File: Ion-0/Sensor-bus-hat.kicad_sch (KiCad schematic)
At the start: 98 parts, among them J10 Conn_CAN, J13 Conn_01x04, J15 Conn_01x04, J6 Coaxial_Small, J7 Conn_Probs, J8 Conn_Heater, Q1 IRLML6244, Q2 IRLML6244, U1 HDC2080, U2 MS5607-02BA, U3 BNO085, U4 TCA9617ADGKR, U5 A4988SETTR-T, U6 MAX-M10M-00B, U7 TPS3850H50DRCR, U8 SN65HVD230, Y2 9HT10-32.768KBZF-T

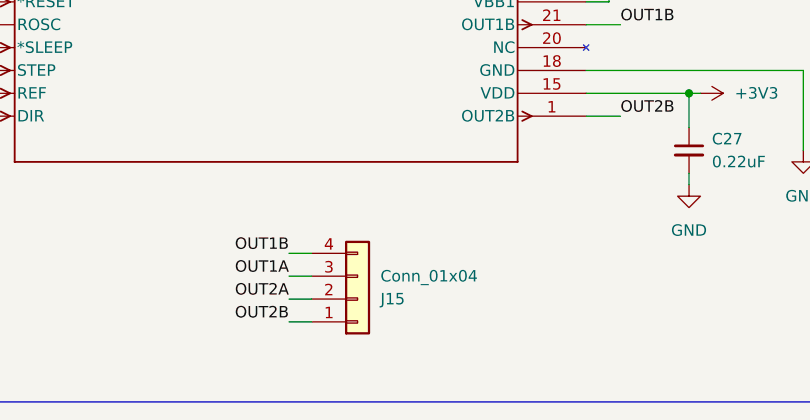
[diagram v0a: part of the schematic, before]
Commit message: silkscreen changes
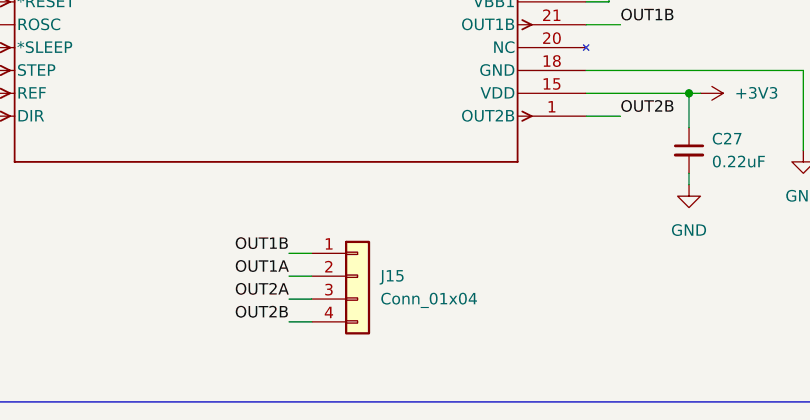
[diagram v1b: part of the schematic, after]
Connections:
- net OUT1A: now also J15.2 (Pin_2); no longer J15.3 (Pin_3)
- net OUT1B: now also J15.1 (Pin_1); no longer J15.4 (Pin_4)
- net OUT2A: now also J15.3 (Pin_3); no longer J15.2 (Pin_2)
- net OUT2B: now also J15.4 (Pin_4); no longer J15.1 (Pin_1)
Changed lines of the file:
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@@
 	(symbol
 		(lib_id "Connector_Generic:Conn_01x04")
-		(at 102.87 270.51 0)
-		(mirror x)
+		(at 102.87 267.97 0)
 		(unit 1)
 		(body_style 1)
@@
 		(dnp no)
 		(property "Reference" "J15"
-			(at 105.41 270.5101 0)
+			(at 105.41 267.9699 0)
 			(show_name no)
 			(do_not_autoplace no)
@@
 		)
 		(property "Value" "Conn_01x04"
-			(at 105.41 267.9701 0)
+			(at 105.41 270.5099 0)
 			(show_name no)
 			(do_not_autoplace no)
@@
 		)
 		(property "Footprint" "Connector_JST:JST_XH_B4B-XH-AM_1x04_P2.50mm_Vertical"
-			(at 102.87 270.51 0)
+			(at 102.87 267.97 0)
 			(hide yes)
 			(show_name no)
@@
 		)
 		(property "Datasheet" ""
-			(at 102.87 270.51 0)
+			(at 102.87 267.97 0)
 			(hide yes)
 			(show_name no)
@@
 		)
 		(property "Description" "Generic connector, single row, 01x04, script generated (kicad-library-utils/schlib/autogen/connector/)"
-			(at 102.87 270.51 0)
+			(at 102.87 267.97 0)
 			(hide yes)
 			(show_name no)

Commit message: fixed impedance mismatch
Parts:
- C11: footprint Capacitor_SMD:C_0603_1608Metric -> Capacitor_SMD:C_0402_1005Metric
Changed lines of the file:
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@@
 			)
 		)
-		(property "Footprint" "Capacitor_SMD:C_0603_1608Metric"
+		(property "Footprint" "Capacitor_SMD:C_0402_1005Metric"
 			(at 198.12 179.07 0)
 			(hide yes)

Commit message: BOM ORDER
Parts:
- removed R12: 523, Resistor_SMD:R_0603_1608Metric_Pad0.98x0.95mm_HandSolder, symbol Device:R_Small_US
- removed R13: 80.6, Resistor_SMD:R_0603_1608Metric_Pad0.98x0.95mm_HandSolder, symbol Device:R_Small_US
- J15, J7: footprint Connector_JST:JST_XH_B4B-XH-AM_1x04_P2.50mm_Vertical -> TerminalBlock:TerminalBlock_Xinya_XY308-2.54-4P_1x04_P2.54mm_Horizontal
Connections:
- net +5V: now also U7.10 (SENSE)
